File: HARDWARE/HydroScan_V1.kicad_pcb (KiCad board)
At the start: 4 copper layers, 202 x 100 mm, 105 parts, among them CN2 DB128V-5.08-2P-GN-S, Q13 2n3904S-RTK/PS_C18536, Q14 2n3904S-RTK/PS_C18536, Q15 2n3904S-RTK/PS_C18536, Q16 2n3904S-RTK/PS_C18536, SW2 BOOT, SW4 RESET, U1 IP2312-4V35, U13 ESP32-WROOM-32D, U14 CH340C, U15 CH340C, U16 ESP32-WROOM-32D, U2 BQ25798RQMR, U2 L298N, U7 LM2576HVS-3.3

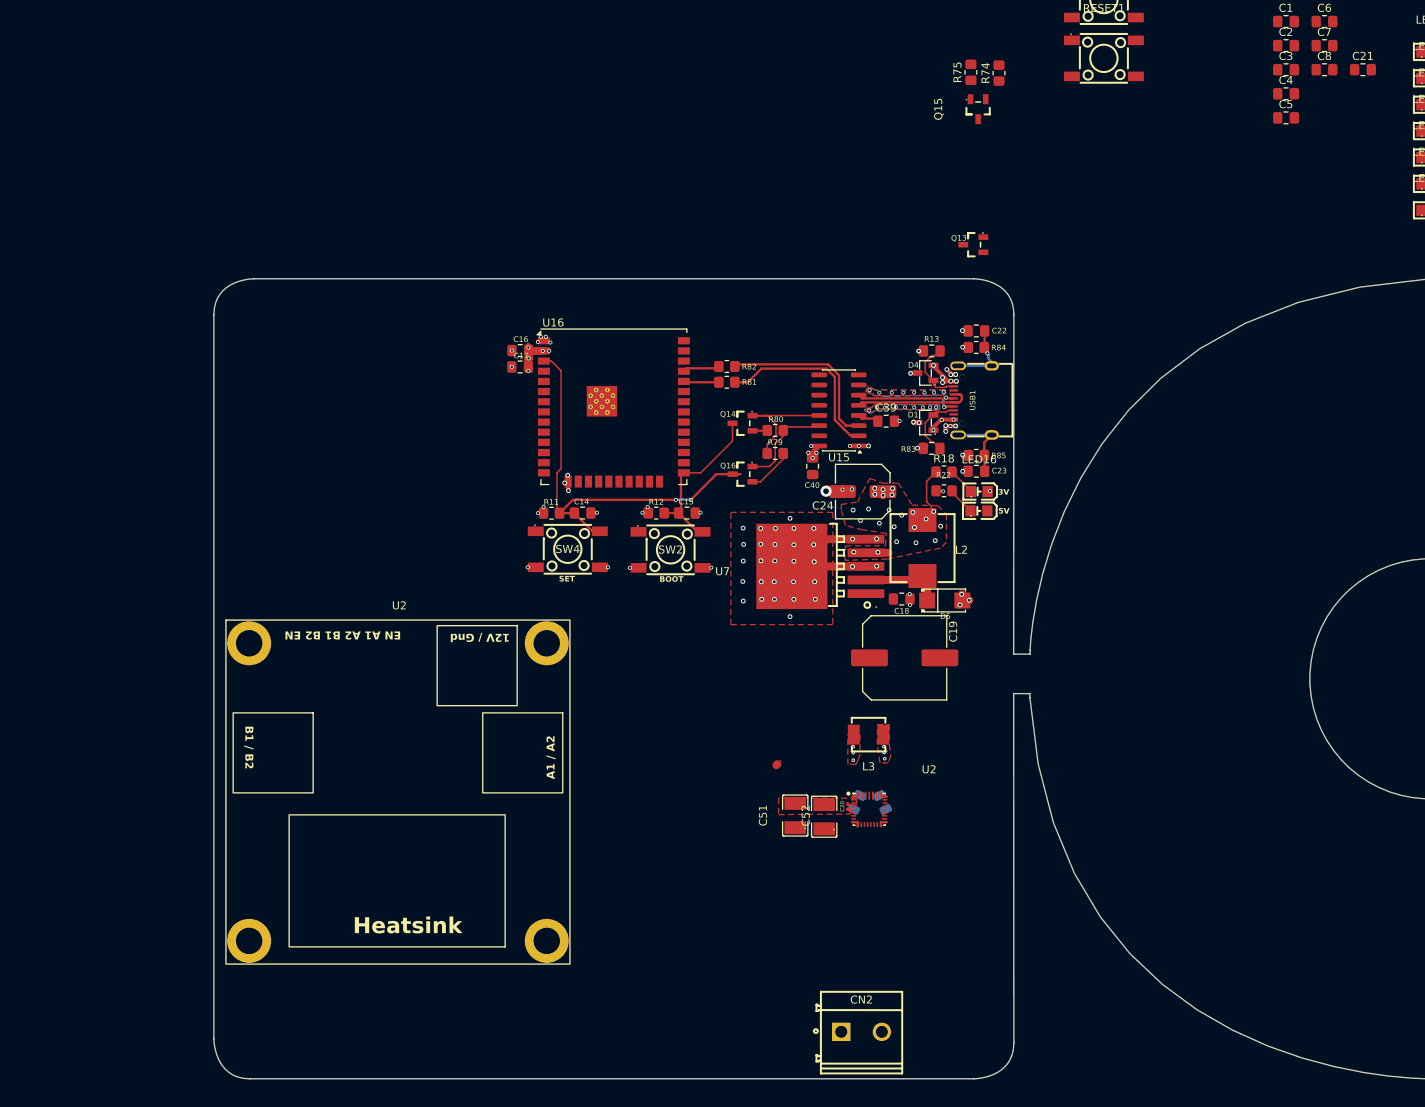
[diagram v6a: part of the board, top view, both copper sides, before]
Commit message: USB c and Fast chargin update finish
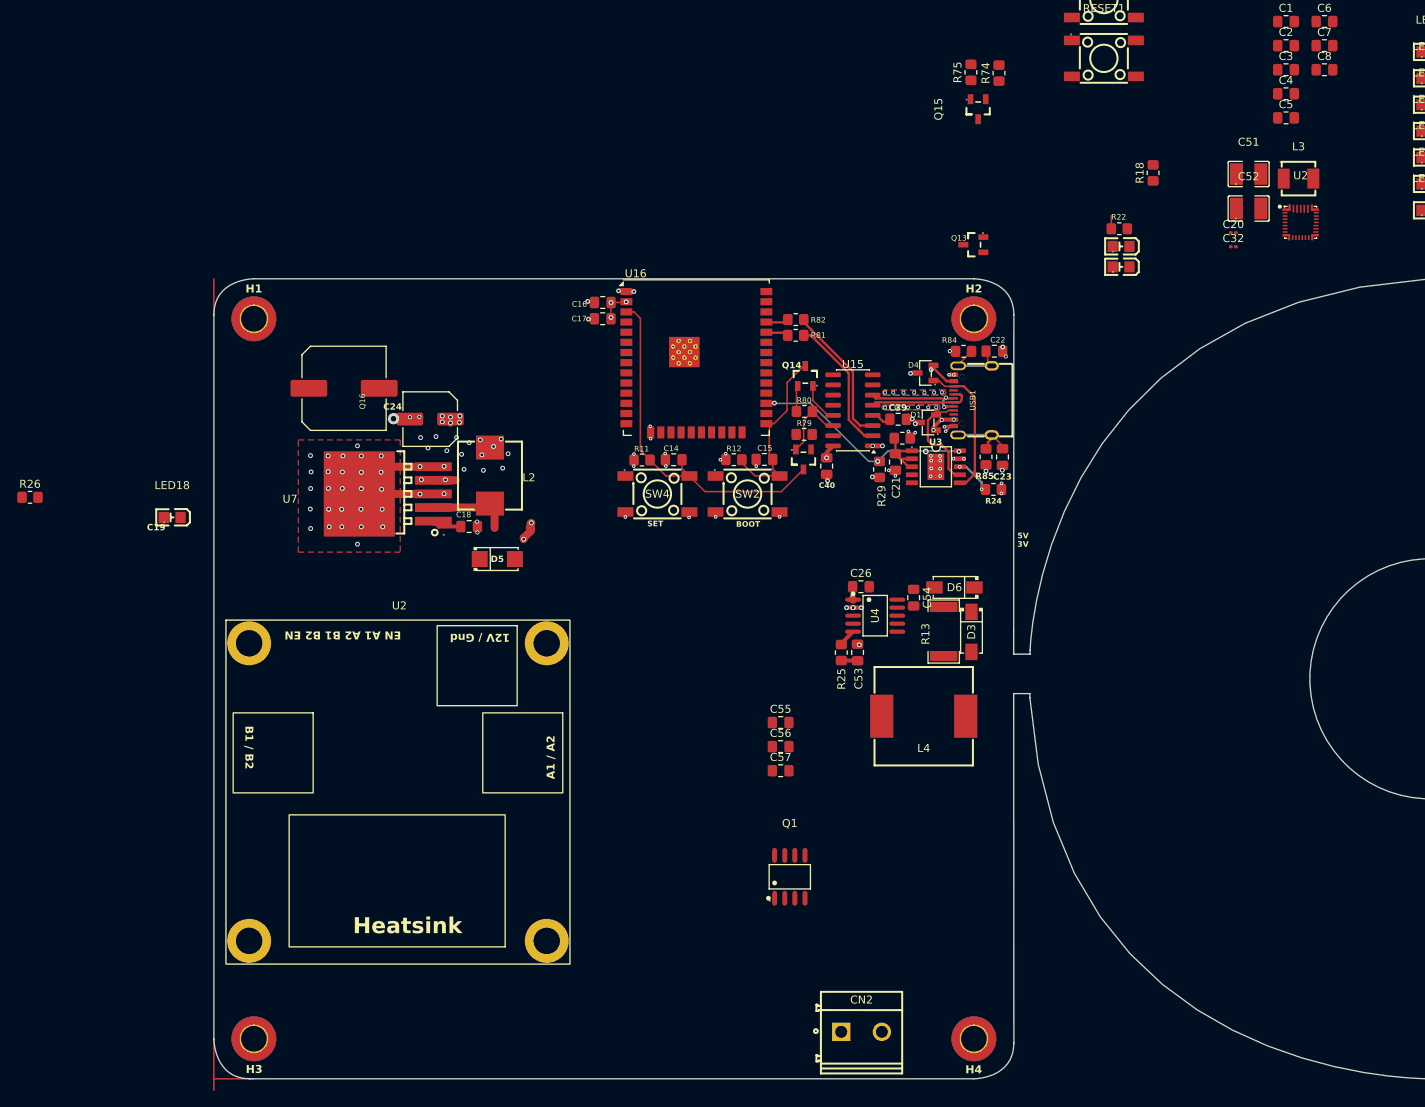
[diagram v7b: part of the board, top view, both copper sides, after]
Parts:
- removed C27, C28: 47nf, Capacitor_SMD:C_0805_2012Metric
- removed R83: 5.11k, Capacitor_SMD:C_0805_2012Metric_Pad1.18x1.45mm_HandSolder
- added C26: 0.1uf, Capacitor_SMD:C_0805_2012Metric_Pad1.18x1.45mm_HandSolder, F.Cu at (160.9, 158.5)
- added C32: 0.1uf, Capacitor_SMD:C_0201_0603Metric, F.Cu at (207.4, 116.0)
- added C53: 220nF, Capacitor_SMD:C_0805_2012Metric_Pad1.18x1.45mm_HandSolder, F.Cu at (160.5, 166.7)
- added C54: 10uF, Capacitor_SMD:C_0805_2012Metric_Pad1.18x1.45mm_HandSolder, F.Cu at (167.5, 159.9)
- added C55: 1uF, Capacitor_SMD:C_0805_2012Metric_Pad1.18x1.45mm_HandSolder, F.Cu at (150.8, 175.5)
- added C56: 10uF, Capacitor_SMD:C_0805_2012Metric_Pad1.18x1.45mm_HandSolder, F.Cu at (150.8, 178.5)
- added C57: 1uF, Capacitor_SMD:C_0805_2012Metric_Pad1.18x1.45mm_HandSolder, F.Cu at (150.8, 181.5)
- added D3: SS54_C22452, EasyEDA:SMA_L4.4-W2.8-LS5.4-R-RD, F.Cu at (174.7, 164.1)
- added D6: SS54_C22452, EasyEDA:SMA_L4.4-W2.8-LS5.4-R-RD, F.Cu at (172.6, 158.6)
- added H1: MountingHole_3.2mm_M3_DIN965_Pad_TopBottom, MountingHole:MountingHole_3.2mm_M3_DIN965_Pad_TopBottom, F.Cu at (85.0, 125.0)
- added H2: MountingHole_3.2mm_M3_DIN965_Pad_TopBottom, MountingHole:MountingHole_3.2mm_M3_DIN965_Pad_TopBottom, F.Cu at (175.0, 125.0)
- added H3: MountingHole_3.2mm_M3_DIN965_Pad_TopBottom, MountingHole:MountingHole_3.2mm_M3_DIN965_Pad_TopBottom, F.Cu at (85.0, 215.0)
- added H4: MountingHole_3.2mm_M3_DIN965_Pad_TopBottom, MountingHole:MountingHole_3.2mm_M3_DIN965_Pad_TopBottom, F.Cu at (175.0, 215.0)
- added L4: SMDRI127-220MT, EasyEDA:IND-SMD_L12.3-W12.3_SMDRI127, F.Cu at (168.7, 174.7)
- added LED18: YLED0805G, EasyEDA:LED0805-FD-GREEN, F.Cu at (74.8, 149.8)
- added Q1: AO4435_C2944310, EasyEDA:SOP-8_L5.0-W3.8-P1.27-LS6.0-BL, F.Cu at (152.0, 194.8)
- added R23: 1k, Resistor_SMD:R_0805_2012Metric_Pad1.20x1.40mm_HandSolder, F.Cu at (166.1, 139.9)
- added R24: 10k, Resistor_SMD:R_0805_2012Metric_Pad1.20x1.40mm_HandSolder, F.Cu at (177.4, 146.3)
- added R25: 120, Resistor_SMD:R_0805_2012Metric_Pad1.20x1.40mm_HandSolder, F.Cu at (158.4, 166.7)
- added R26: 2.2k, Resistor_SMD:R_0805_2012Metric_Pad1.20x1.40mm_HandSolder, F.Cu at (57.0, 147.3)
- added R29: 10k, Resistor_SMD:R_0805_2012Metric_Pad1.20x1.40mm_HandSolder, F.Cu at (163.2, 143.8)
- added REF**: WEEE-Logo_5.6x8mm_SilkScreen, Symbol:WEEE-Logo_5.6x8mm_SilkScreen, B.Cu at (164.7, 124.6)
- added U3: CH224K, EasyEDA:ESSOP-10_L4.9-W3.9-P1.0-LS6.0-TL-EP, F.Cu at (170.2, 143.5)
- added U4: CN3795, EasyEDA:SSOP-10_L4.9-W3.9-P1.00-LS6.0-BL, F.Cu at (162.7, 162.1)
- C21: value 10uf -> 1uf
- R13: value 5.11k -> YLRY12-3-60F; footprint Capacitor_SMD:C_0805_2012Metric_Pad1.18x1.45mm_HandSolder -> EasyEDA:R2512
- moved C51 98.2 mm to (209.3, 106.9), turned to 0 degrees
- moved C52 92.7 mm to (209.3, 111.2), turned to 0 degrees
- moved U2 91.1 mm to (215.8, 113.0)
- moved L3 87.9 mm to (215.6, 107.5), turned to 0 degrees
- moved C20 86.4 mm to (207.4, 114.2), turned to 0 degrees
- moved C19 77.8 mm to (96.3, 133.7)
- moved C21 76.3 mm to (165.2, 142.9), turned to -90 degrees
- moved D5 56.2 mm to (115.4, 155.0)
- moved C24 54.8 mm to (107.0, 137.5)
- moved L2 54.8 mm to (114.5, 144.6)
- moved C18 54.8 mm to (111.9, 151.0)
- moved U7 54.8 mm to (102.8, 146.9)
- moved R18 45.6 mm to (197.4, 106.8), turned to 90 degrees
- moved R22 39.4 mm to (193.2, 113.7)
- moved LED16 35.4 mm to (193.4, 116.0)
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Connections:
- C21 pad 1: GND -> /VDD
- C21 pad 2: /VAC1 -> GND
- C40 pad 1: /V5_1 -> 3.3V
- R13 pad 1: GND -> /CSP
- R13 pad 2: /CC2_1 -> /1
- U15 pad 16: /V5_1 -> 3.3V
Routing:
- net /IO16_1: track 0.00 -> 28.0 mm, vias 0 -> 3
- net /DTR_1: track 17.0 -> 5.11 mm
- net GND: track 51.5 -> 62.8 mm, vias 92 -> 105
- net /CC2_1: track 8.42 -> 18.0 mm
- net /VDD: track 0.00 -> 9.32 mm
- net /EN: track 51.5 -> 44.7 mm, vias 2 -> 0
- net Net-(Q16-B): track 5.71 -> 0.00 mm
- net Net-(U15-TXD): track 22.8 -> 17.2 mm
- net /CC1_1: track 8.36 -> 13.4 mm
- net Net-(U3-VBUS): track 0.00 -> 4.90 mm, vias 0 -> 2
- net Net-(U15-RXD): track 21.9 -> 17.1 mm
- net 3.3V: track 24.4 -> 19.6 mm, vias 32 -> 24
- net /SYS: track 0.10 -> 3.81 mm
- net Net-(LED17-A): track 3.47 -> 0.00 mm
- net Net-(LED16-A): track 3.24 -> 0.00 mm
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- removed copper zone on F.Cu, net /SW1
- removed copper zone on F.Cu, net /SW2
- removed copper zone on F.Cu, net /VAC1
- removed copper zone on F.Cu, net 3.3V

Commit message: power updating
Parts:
- removed C33, C34, C35: 25TQC33MYF, EasyEDA:CAP-SMD_L7.3-W4.3-FD
- removed C51, C52: CL32B106KBJNNNE, EasyEDA:C1210
- removed CN2: DB128V-5.08-2P-GN-S, EasyEDA:CONN-TH_2P-P5.08_DIBO_DB128V-5.08
- removed JP1, JP2, JP3, JP4, JP5: SolderJumper_2_Open, Jumper:SolderJumper-2_P1.3mm_Open_RoundedPad1.0x1.5mm
- removed L3: 0420CDMCCDS-1R0MC, EasyEDA:IND-SMD_L4.2-W4.2_MCW-0420
- removed LED14: YLED0805G, EasyEDA:LED0805-FD-GREEN
- removed R16: 2.2k, Resistor_SMD:R_0805_2012Metric_Pad1.20x1.40mm_HandSolder
- removed R21: 100, Resistor_SMD:R_0805_2012Metric_Pad1.20x1.40mm_HandSolder
- added C57: 1uF, Capacitor_SMD:C_0805_2012Metric_Pad1.18x1.45mm_HandSolder, F.Cu at (144.5, 188.4)
- added C58: CA45-D035K226T, EasyEDA:CAP-SMD_L7.3-W4.3-R-RD, F.Cu at (59.1, 190.3)
- added CN3: DB128V-5.08-2P-GN-S, EasyEDA:CONN-TH_2P-P5.08_DIBO_DB128V-5.08, F.Cu at (72.0, 163.4)
- added D7: SS54_C22452, EasyEDA:SMA_L4.4-W2.8-LS5.4-R-RD, F.Cu at (149.2, 187.1)
- added D8: SS54_C22452, EasyEDA:SMA_L4.4-W2.8-LS5.4-R-RD, F.Cu at (149.2, 190.0)
- added LED18: YLED0805G, EasyEDA:LED0805-FD-GREEN, F.Cu at (147.5, 192.8)
- added M_N1: M_N, Connector_PinHeader_2.00mm:PinHeader_1x01_P2.00mm_Vertical, F.Cu at (95.2, 188.8)
- added M_P1: TestPoint, Connector_PinHeader_2.00mm:PinHeader_1x01_P2.00mm_Vertical, F.Cu at (95.2, 182.9)
- added R31: 2.2k, Resistor_SMD:R_0805_2012Metric_Pad1.20x1.40mm_HandSolder, F.Cu at (157.4, 188.2)
- added U10: DB125-3.81-2P-BK-S, EasyEDA:CONN-TH_2P-P3.81_DB125-3.81-2P-BK-S, F.Cu at (83.9, 178.7)
- added U11: DB125-3.81-2P-BK-S, EasyEDA:CONN-TH_2P-P3.81_DB125-3.81-2P-BK-S, F.Cu at (165.9, 215.9)
- added U8: DB125-3.81-2P-BK-S, EasyEDA:CONN-TH_2P-P3.81_DB125-3.81-2P-BK-S, F.Cu at (83.9, 196.1)
- added U9: DB125-3.81-2P-BK-S, EasyEDA:CONN-TH_2P-P3.81_DB125-3.81-2P-BK-S, F.Cu at (83.9, 187.4)
- C20: value 0.1uf -> CA45-D035K226T; footprint Capacitor_SMD:C_0201_0603Metric -> EasyEDA:CAP-SMD_L7.3-W4.3-R-RD
- C39: value 100nf -> RVT1V101M0607; footprint Capacitor_SMD:C_0805_2012Metric_Pad1.18x1.45mm_HandSolder -> EasyEDA:CAP-SMD_BD6.3-L6.6-W6.6-LS7.6-FD
- C55: value 1uF -> 0.1uf
- moved U1 168.8 mm to (312.1, 129.9)
- moved R2 165.3 mm to (300.9, 103.6)
- moved R3 165.3 mm to (300.9, 106.6)
- moved R4 165.3 mm to (300.9, 109.5)
- moved R10 164.0 mm to (305.6, 103.6)
- moved R14 164.0 mm to (305.6, 106.6)
- moved R9 164.0 mm to (305.6, 100.7)
- moved R17 163.8 mm to (305.6, 112.5)
- moved U14 163.7 mm to (299.3, 120.1)
- moved SGM2212-3.1 157.9 mm to (289.0, 133.1)
- moved L1 150.0 mm to (298.3, 134.9)
- moved USB2 145.3 mm to (301.7, 129.0)
- moved R6 142.3 mm to (300.9, 112.5)
- moved R1 141.1 mm to (300.9, 100.7)
- moved R15 140.9 mm to (305.6, 109.5)
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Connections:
- C18 pad 1: /SYS -> /VCC_REG
- C19 pad 1: /SYS -> /VCC_REG
- C20 pad 1: /VAC1 -> /1
- C26 pad 2: unconnected-(C26-Pad2) -> /V5_1
- C39 pad 1: /V3_1 -> /V5_1
- D6 pad 1: /V5_1 -> /DRAIN
- Q1 pad 1: /SOURSE -> /V5_1
- Q1 pad 2: /SOURSE -> /V5_1
- Q1 pad 3: /SOURSE -> /V5_1
- U15 pad 4: /V3_1 -> 3.3V
- U2 pad 1: /STAT -> unconnected-(U2-STAT-Pad1)
- U2 pad 10: GND -> unconnected-(U2-ACDRV2-Pad10)
- U2 pad 11: GND -> unconnected-(U2-ACDRV1-Pad11)
- U2 pad 13: Net-(JP5-A) -> unconnected-(U2-~{CE}-Pad13)
- U2 pad 16: /TS -> unconnected-(U2-TS-Pad16)
- U2 pad 17: Net-(U2-ILIM_HIZ) -> unconnected-(U2-ILIM_HIZ-Pad17)
- U2 pad 18: /BATP -> unconnected-(U2-BATP-Pad18)
- U2 pad 19: /BTST2 -> unconnected-(U2-BTST2-Pad19)
- U2 pad 2: /VAC1 -> unconnected-(U2-VBUS-Pad2)
- U2 pad 20: Net-(U2-PROG) -> unconnected-(U2-PROG-Pad20)
- U2 pad 23: /<NO NET> -> unconnected-(U2-BAT-Pad23)
- U2 pad 24: /SDRV -> unconnected-(U2-SDRV-Pad24)
- U2 pad 25: /SYS -> unconnected-(U2-SYS-Pad25)
- U2 pad 26: /SW2 -> unconnected-(U2-SW2-Pad26)
- U2 pad 27: GND -> unconnected-(U2-GND-Pad27)
- U2 pad 28: /SW1 -> unconnected-(U2-SW1-Pad28)
- U2 pad 29: Net-(U2-PMID) -> unconnected-(U2-PMID-Pad29)
- U2 pad 3: /VAC1 -> unconnected-(U2-VBUS-Pad3)
- U2 pad 4: /BTST1 -> unconnected-(U2-BTST1-Pad4)
- U2 pad 5: /REGN -> unconnected-(U2-REGN-Pad5)
- U2 pad 8: /VAC2 -> unconnected-(U2-VAC2-Pad8)
- U2 pad 9: /VAC1 -> unconnected-(U2-VAC1-Pad9)
- U4 pad 3: unconnected-(U4-nCHRG-Pad3) -> /CHARG
- U4 pad 4: unconnected-(U4-MPPT-Pad4) -> Net-(U4-MPPT)
- U7 pad 1: /SYS -> /VCC_REG
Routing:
- net /1: track 0.00 -> 69.8 mm, vias 0 -> 12
- net /CSP: track 0.00 -> 18.8 mm
- net /V5_1: track 13.1 -> 31.3 mm, vias 8 -> 20
- net 3.3V: track 19.6 -> 28.6 mm
- net GND: track 62.8 -> 71.7 mm, vias 105 -> 124
- net Net-(Q1-G): track 0.00 -> 6.24 mm, vias 0 -> 2
- net /SYS: track 3.81 -> 0.00 mm
- net /VCC_REG: track 0.00 -> 3.81 mm
- net Net-(LED18-A): track 0.00 -> 3.11 mm
- net Net-(U4-VG): track 0.08 -> 2.60 mm
- net Net-(U4-COM): track 2.22 -> 0.00 mm
- net /V3_1: track 2.09 -> 0.00 mm
- net Net-(C53-Pad2): track 2.04 -> 0.00 mm
- net /DRAIN: vias 0 -> 1
- added copper zone on F.Cu, net /1
- added copper zone on F.Cu, net /DRAIN
- added copper zone on In2.Cu, net /V_BATTERY__1
- added copper zone on F.Cu, net Net-(D3-K)
- added copper zone on In2.Cu, net Net-(M_N1-Pad1)
- added copper zone on In2.Cu, net Net-(M_P1-Pad1)
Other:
- board text added: "+"
- board text added: "-"
- board text added: "A"
- board text added: "BATERY"
- board text added: "N"
- board text added: "P"
- board text added: "V"
